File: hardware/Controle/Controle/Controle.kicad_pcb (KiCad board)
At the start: 2 copper layers, 70 x 50 mm, 62 parts, among them J101 USART, J102 ST_LINK, J103 FAN, J104 Switches, J301 RJ45, Q101 BCV27, U201 MCP2561-E-SN, U401 AP1117-3.3, U402 AP1117-5, U403 AP1117-15, U501 STM32F103C8Tx, Y501 8mhz

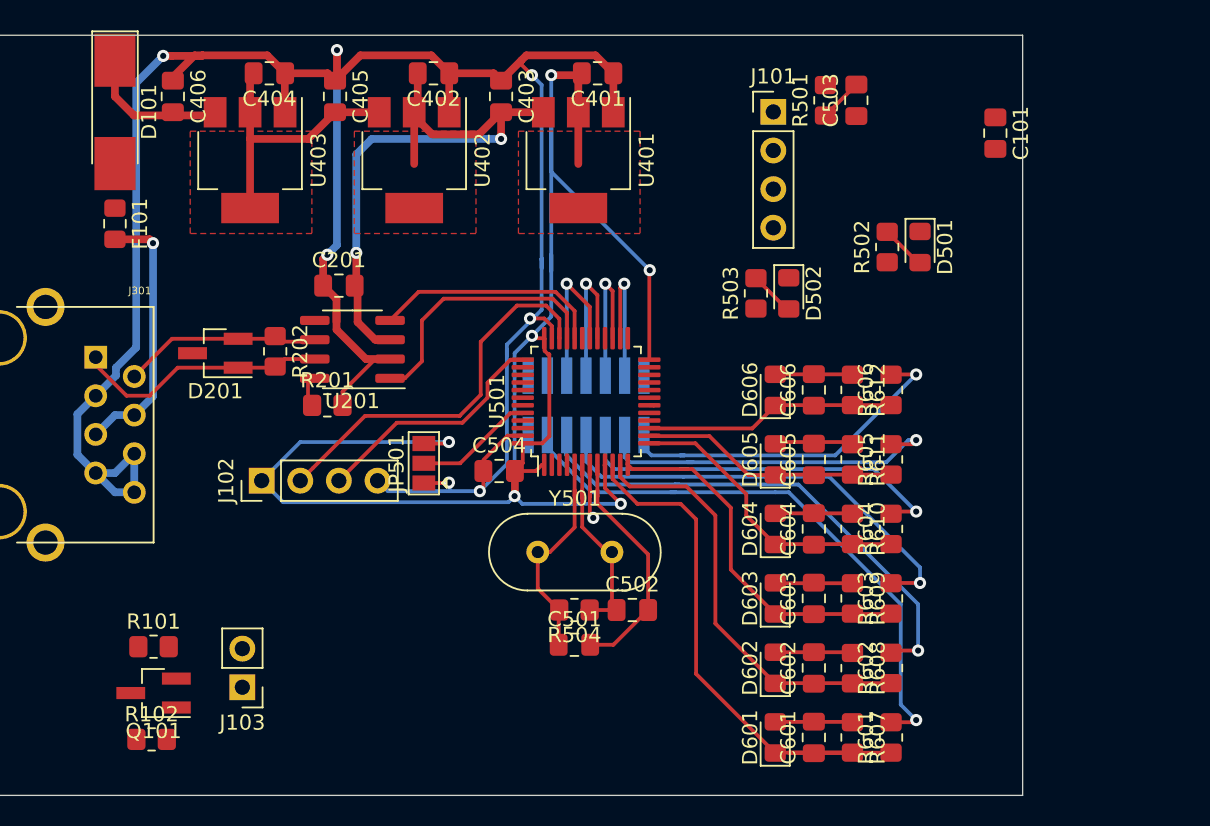
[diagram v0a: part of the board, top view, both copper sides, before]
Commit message: adicionado o TL7726 e modificada a placa
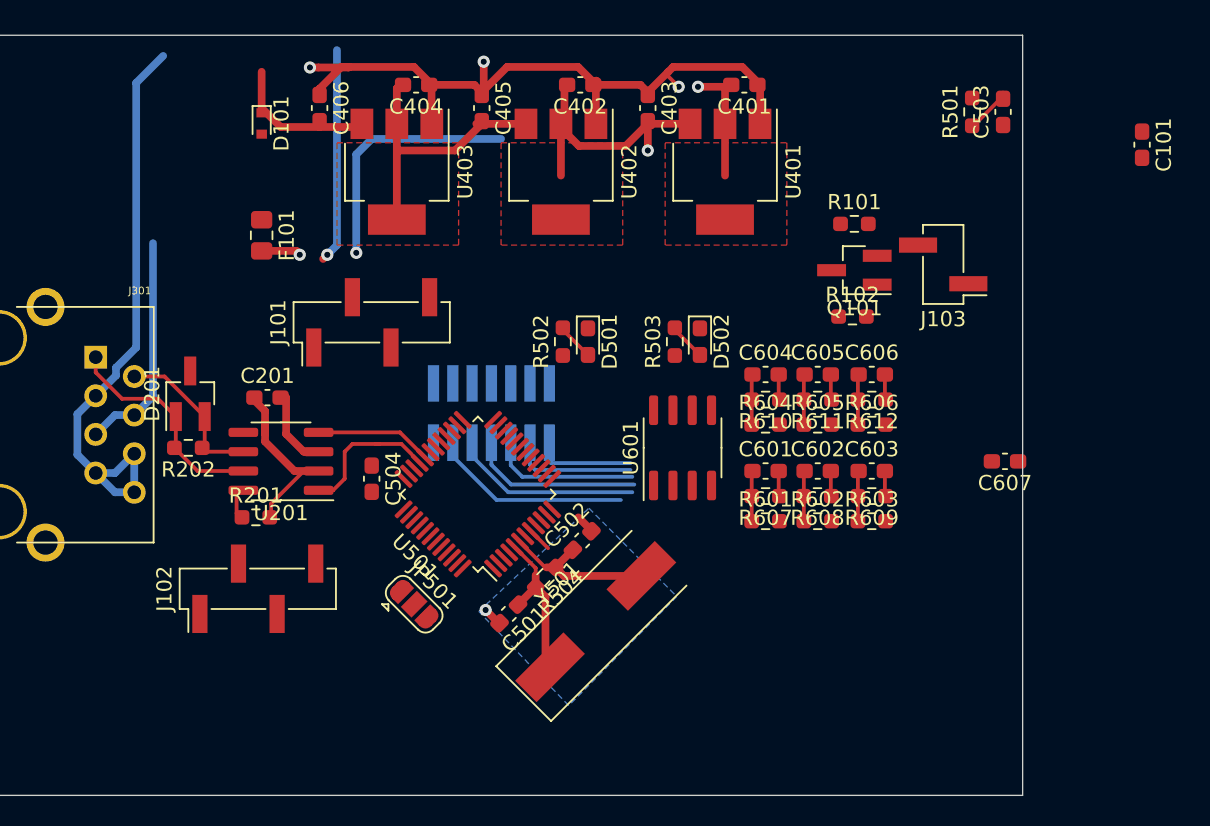
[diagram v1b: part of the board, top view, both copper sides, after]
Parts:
- removed D601, D602, D603, D604, D605, D606: 3v3, Diode_SMD:D_0805_2012Metric_Pad1.15x1.40mm_HandSolder
- added C607: 100n, Capacitor_SMD:C_0603_1608Metric_Pad1.08x0.95mm_HandSolder, F.Cu at (194.6, 73.5)
- added U601: TL7726IDR, Package_SO:SOIC-8_3.9x4.9mm_P1.27mm, F.Cu at (173.4, 72.6)
- C101, C201, C401, C402, C403, C404, C405, C406, C501, C502, C503, C504, C601, C602, C603, C604, C605, C606: footprint Capacitor_SMD:C_0805_2012Metric_Pad1.18x1.45mm_HandSolder -> Capacitor_SMD:C_0603_1608Metric_Pad1.08x0.95mm_HandSolder
- D101: footprint Diode_SMD:D_MELF_Handsoldering -> Diode_SMD:D_SOD-523
- D501, D502: footprint LED_SMD:LED_0805_2012Metric_Pad1.15x1.40mm_HandSolder -> LED_SMD:LED_0603_1608Metric_Pad1.05x0.95mm_HandSolder
- J101, J102: footprint Connector_PinHeader_2.54mm:PinHeader_1x04_P2.54mm_Vertical -> Connector_PinHeader_2.54mm:PinHeader_1x04_P2.54mm_Vertical_SMD_Pin1Left
- J103: footprint Connector_PinHeader_2.54mm:PinHeader_1x02_P2.54mm_Vertical -> Connector_PinHeader_2.54mm:PinHeader_1x02_P2.54mm_Vertical_SMD_Pin1Left
- JP501: footprint Jumper:SolderJumper-3_P1.3mm_Open_Pad1.0x1.5mm -> Jumper:SolderJumper-3_P1.3mm_Open_RoundedPad1.0x1.5mm
- R101, R102, R201, R202, R501, R502, R503, R504, R601, R602, R603, R604, R605, R606, R607, R608, R609, R610, R611, R612: footprint Resistor_SMD:R_0805_2012Metric_Pad1.20x1.40mm_HandSolder -> Resistor_SMD:R_0603_1608Metric_Pad0.98x0.95mm_HandSolder
- Y501: footprint Crystal:Crystal_HC49-U_Vertical -> Crystal:Crystal_SMD_HC49-SD
- moved R102 53.8 mm to (184.5, 64.0)
- moved J103 53.8 mm to (190.5, 60.6)
- moved Q101 53.8 mm to (184.7, 61.0)
- moved R101 53.8 mm to (184.7, 57.9)
- moved J101 29.8 mm to (152.9, 64.4), turned to 90 degrees
- moved D501 22.7 mm to (167.1, 65.7)
- moved R502 22.2 mm to (165.5, 65.7)
- moved C601 17.8 mm to (178.8, 74.2), turned to 0 degrees
- moved R607 16.9 mm to (178.8, 75.8), turned to 180 degrees
- moved R601 16.4 mm to (178.8, 77.5), turned to 0 degrees
- moved C602 13.0 mm to (182.2, 74.2), turned to 0 degrees
- moved R608 11.6 mm to (182.2, 75.8), turned to 180 degrees
- moved R602 10.8 mm to (182.2, 77.5), turned to 0 degrees
- moved R604 10.7 mm to (178.8, 71.1), turned to 0 degrees
- moved C604 10.6 mm to (178.8, 67.8), turned to 0 degrees
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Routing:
- net +3V3: track 114.7 -> 8.13 mm, vias 6 -> 1
- net GND: track 209.9 -> 127.8 mm, vias 7 -> 5
- net /STM32/ADC1_IN0: track 37.3 -> 3.53 mm
- net /STM32/ADC1_IN1: track 28.9 -> 3.25 mm
- net /STM32/SWCLK: track 25.5 -> 0.00 mm
- net /analog/In0: track 38.4 -> 13.1 mm, vias 1 -> 0
- net /analog/In1: track 33.8 -> 12.4 mm, vias 1 -> 0
- net /STM32/ADC1_IN2: track 24.4 -> 3.40 mm
- net /analog/In2: track 29.5 -> 11.4 mm, vias 1 -> 0
- net /STM32/ADCX_IN3: track 19.5 -> 3.25 mm
- net /STM32/SWDIO: track 16.1 -> 0.00 mm
- net /analog/In3: track 25.6 -> 9.80 mm, vias 1 -> 0
- net /analog/In5: track 23.1 -> 7.83 mm, vias 1 -> 0
- net /analog/In4: track 23.5 -> 8.30 mm, vias 1 -> 0
- net /STM32/ADCX_IN4: track 17.0 -> 3.25 mm
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- added copper zone on B.Cu, net GND

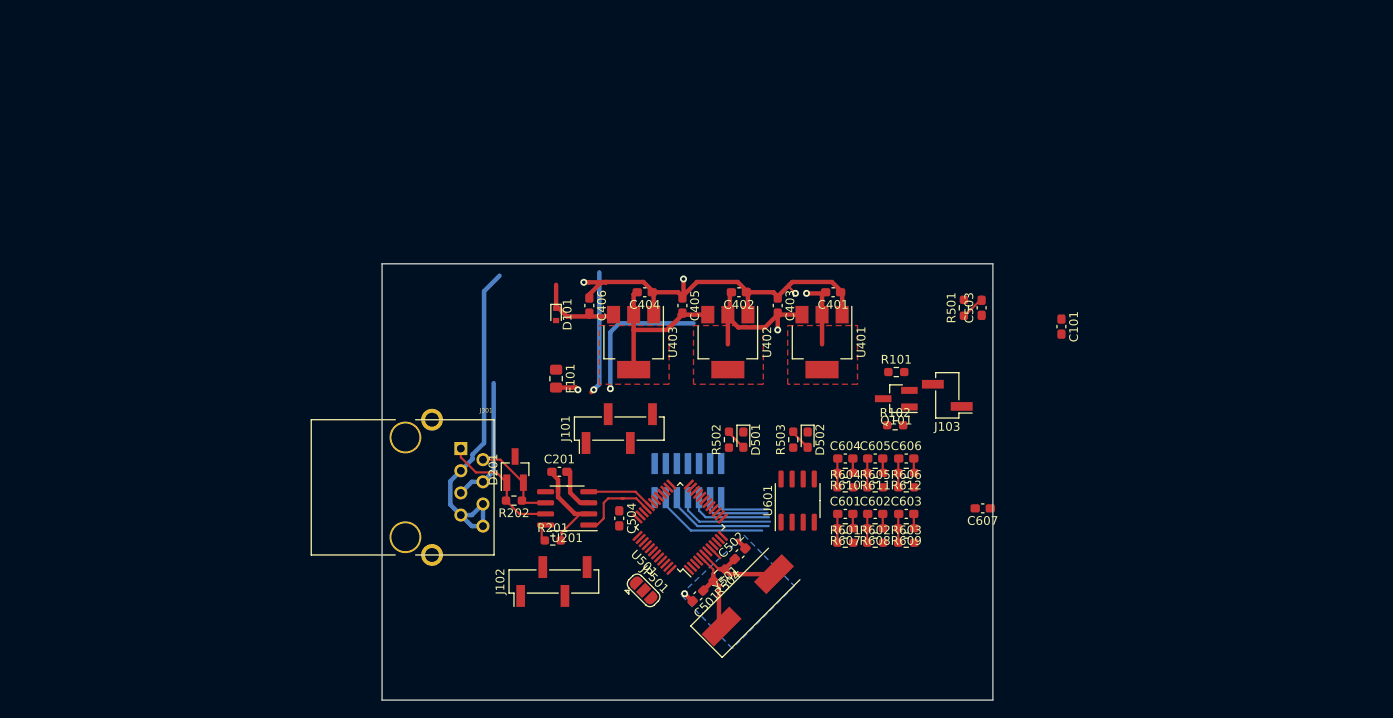
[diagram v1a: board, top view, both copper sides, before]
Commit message: control PCB updated
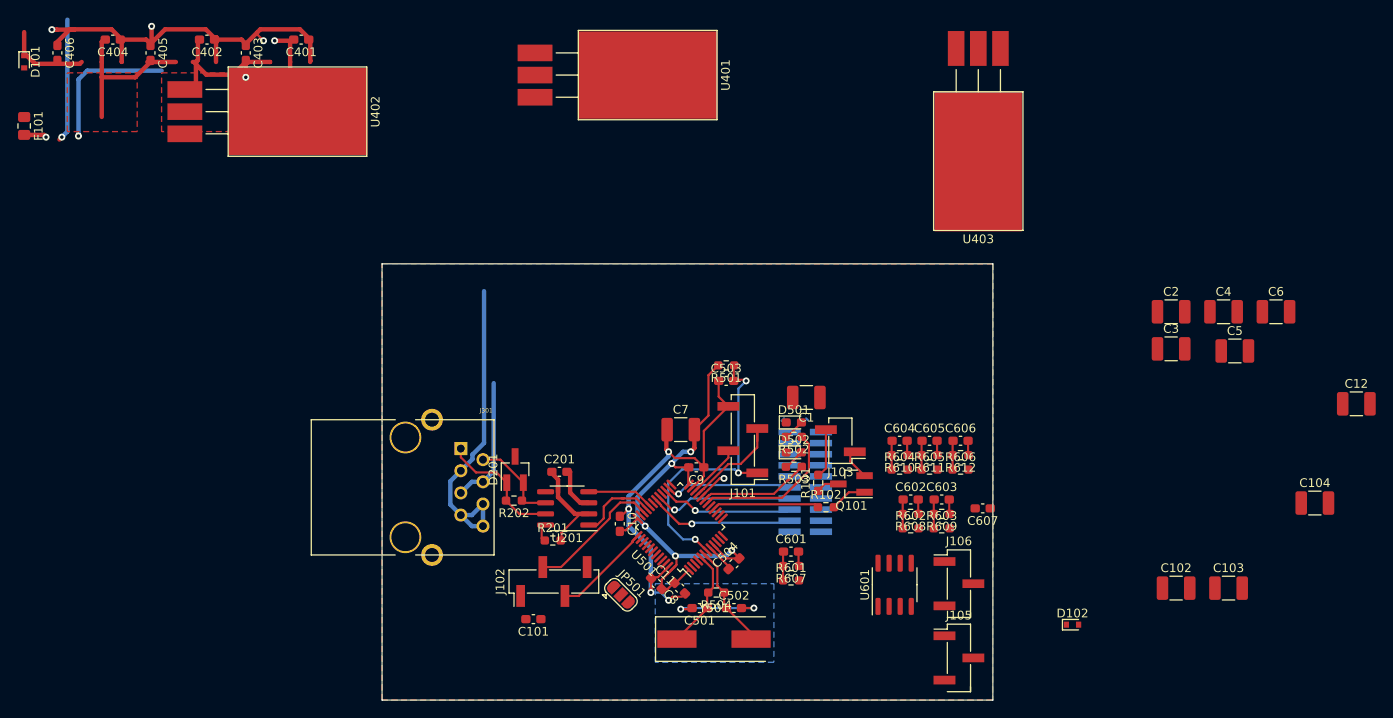
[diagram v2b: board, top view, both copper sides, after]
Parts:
- removed J104: Switches, Connector_PinHeader_1.27mm:PinHeader_2x07_P1.27mm_Vertical_SMD
- added C1: 4.7u, Capacitor_SMD:C_1210_3225Metric_Pad1.33x2.70mm_HandSolder, F.Cu at (174.3, 60.8)
- added C10: 100n, Capacitor_SMD:C_0603_1608Metric_Pad1.08x0.95mm_HandSolder, F.Cu at (153.0, 75.3)
- added C102: 4.7u, Capacitor_SMD:C_1210_3225Metric_Pad1.33x2.70mm_HandSolder, F.Cu at (216.7, 82.7)
- added C103: 4.7u, Capacitor_SMD:C_1210_3225Metric_Pad1.33x2.70mm_HandSolder, F.Cu at (222.7, 82.7)
- added C104: 4.7u, Capacitor_SMD:C_1210_3225Metric_Pad1.33x2.70mm_HandSolder, F.Cu at (232.6, 72.9)
- added C11: 100n, Capacitor_SMD:C_0603_1608Metric_Pad1.08x0.95mm_HandSolder, F.Cu at (157.2, 82.2)
- added C12: 4.7u, Capacitor_SMD:C_1210_3225Metric_Pad1.33x2.70mm_HandSolder, F.Cu at (237.4, 61.6)
- added C2: 4.7u, Capacitor_SMD:C_1210_3225Metric_Pad1.33x2.70mm_HandSolder, F.Cu at (216.2, 51.0)
- added C3: 4.7u, Capacitor_SMD:C_1210_3225Metric_Pad1.33x2.70mm_HandSolder, F.Cu at (216.2, 55.3)
- added C4: 4.7u, Capacitor_SMD:C_1210_3225Metric_Pad1.33x2.70mm_HandSolder, F.Cu at (222.2, 51.0)
- added C5: 4.7u, Capacitor_SMD:C_1210_3225Metric_Pad1.33x2.70mm_HandSolder, F.Cu at (223.5, 55.5)
- added C6: 4.7u, Capacitor_SMD:C_1210_3225Metric_Pad1.33x2.70mm_HandSolder, F.Cu at (228.2, 51.0)
- added C7: 4.7u, Capacitor_SMD:C_1210_3225Metric_Pad1.33x2.70mm_HandSolder, F.Cu at (160.0, 64.5)
- added C8: 100n, Capacitor_SMD:C_0603_1608Metric_Pad1.08x0.95mm_HandSolder, F.Cu at (159.8, 82.7)
- added C9: 100n, Capacitor_SMD:C_0603_1608Metric_Pad1.08x0.95mm_HandSolder, F.Cu at (161.7, 68.8)
- added D102: LL4148, Diode_SMD:D_SOD-523, F.Cu at (204.9, 86.9)
- added J105: Iin_sen, Connector_PinHeader_2.54mm:PinHeader_1x03_P2.54mm_Vertical_SMD_Pin1Left, F.Cu at (191.8, 90.7)
- added J106: Iin_sen, Connector_PinHeader_2.54mm:PinHeader_1x03_P2.54mm_Vertical_SMD_Pin1Left, F.Cu at (191.8, 82.2)
- added J107: Driver-Sense, KicadZeniteSolarLibrary18:PinSocket_2x10_P1.27mm_Vertical_SMD, B.Cu at (174.2, 70.5)
- U401, U402, U403: footprint Package_TO_SOT_SMD:SOT-223-3_TabPin2 -> KicadZeniteSolarLibrary18:TO-220-3_Horizontal_TabDown_SMD
- moved C101 69.2 mm to (143.1, 86.2), turned to 180 degrees
- moved C401 67.5 mm to (116.5, 19.8)
- moved C404 67.5 mm to (94.9, 19.8)
- moved C406 67.5 mm to (88.5, 21.3)
- moved D101 67.5 mm to (84.7, 22.4)
- moved F101 67.5 mm to (84.7, 29.7)
- moved U402 67.5 mm to (104.4, 25.5)
- moved C402 67.5 mm to (105.7, 19.8)
- moved C403 67.5 mm to (110.1, 21.3)
- moved C405 67.5 mm to (99.2, 21.3)
- moved U403 53.1 mm to (196.6, 22.1), turned to 180 degrees
- moved U401 45.8 mm to (144.5, 21.3)
- moved C503 30.4 mm to (165.2, 58.9), turned to 0 degrees
- moved R501 28.0 mm to (165.2, 57.1), turned to 180 degrees
- moved R101 15.5 mm to (175.7, 70.6), turned to 90 degrees
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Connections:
- R601 pad 2: /analog/In0 -> /SL1_sen
- R602 pad 2: /analog/In1 -> /SL2_sen
- R603 pad 2: /analog/In2 -> /Vin_sen
- R604 pad 2: /analog/In3 -> /Temp1
- R605 pad 2: /analog/In4 -> /Iin_sen
- R606 pad 2: /analog/In5 -> /Iout_sen
- U501 pad 26: /STM32/TIM1_CH1N -> /PWM_L1
- U501 pad 27: /STM32/TIM1_CH2N -> /PWM_L2
- U501 pad 29: /STM32/TIM1_CH1 -> /PWM_H1
- U501 pad 30: /STM32/TIM1_CH2 -> /PWM_H2
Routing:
- net GND: track 127.8 -> 194.8 mm, vias 5 -> 11
- net +3V3: track 8.13 -> 65.3 mm, vias 1 -> 6
- net /STM32/RESET: track 3.11 -> 35.3 mm, vias 0 -> 3
- net /STM32/LED0: track 0.00 -> 17.8 mm
- net /PWM_H2: track 0.00 -> 16.7 mm, vias 0 -> 1
- net +5V: track 39.9 -> 23.5 mm, vias 2 -> 1
- net /Powersupply/+18V: track 9.58 -> 26.0 mm, vias 0 -> 1
- net /PWM_H1: track 0.00 -> 16.1 mm, vias 0 -> 1
- net /STM32/SWCLK: track 0.00 -> 15.7 mm
- net /PWM_L1: track 0.00 -> 14.7 mm, vias 0 -> 1
- net /PWM_L2: track 0.00 -> 14.7 mm, vias 0 -> 1
- net /STM32/LED1: track 0.00 -> 13.2 mm
- net /analog/In0: track 13.1 -> 0.00 mm
- net /STM32/USART3_TX: track 0.00 -> 12.6 mm
- net /analog/In1: track 12.4 -> 0.00 mm
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- added copper zone on F.Cu, net GND

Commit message: Update Controle PCB
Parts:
- removed C501, C502: 20p, Capacitor_SMD:C_0603_1608Metric_Pad1.08x0.95mm_HandSolder
- removed R504: 10k, Resistor_SMD:R_0603_1608Metric_Pad0.98x0.95mm_HandSolder
- removed Y501: 8mhz, Crystal:Crystal_SMD_HC49-SD
- D101, D102: value LL4148 -> B0530W; footprint Diode_SMD:D_SOD-523 -> Diode_SMD:D_SOD-123F
- J102: footprint Connector_PinHeader_2.54mm:PinHeader_1x04_P2.54mm_Vertical_SMD_Pin1Left -> Connector_PinHeader_2.54mm:PinHeader_1x05_P2.54mm_Vertical_SMD_Pin1Left
- U401: value AP1117-3.3 -> AMS1117-3.3; footprint KicadZeniteSolarLibrary18:TO-220-3_Horizontal_TabDown_SMD -> Package_TO_SOT_SMD:SOT-223-3_TabPin2
- U402: value AP1117-5 -> AMS1117-5; footprint KicadZeniteSolarLibrary18:TO-220-3_Horizontal_TabDown_SMD -> Package_TO_SOT_SMD:SOT-223-3_TabPin2
- U403: value AP1117-15 -> K78L15-1000R3; footprint KicadZeniteSolarLibrary18:TO-220-3_Horizontal_TabDown_SMD -> KicadZeniteSolarLibrary18:TO-220-3_Horizontal_Tabless_SMD
- U501: value STM32F103C8Tx -> STM32G431CBT6
- moved U402 76.5 mm to (173.9, 57.4)
- moved C406 65.0 mm to (150.3, 41.5)
- moved C404 64.7 mm to (155.6, 42.2)
- moved C405 61.4 mm to (158.6, 37.1)
- moved U403 60.3 mm to (143.1, 49.8), turned to 270 degrees
- moved D101 59.7 mm to (134.1, 55.9), turned to 0 degrees
- moved C104 58.9 mm to (174.2, 65.3), turned to 180 degrees
- moved F101 57.0 mm to (133.9, 58.5), turned to 0 degrees
- moved C402 52.3 mm to (154.4, 38.9)
- moved C403 44.7 mm to (152.7, 34.9)
- moved C401 41.6 mm to (155.6, 33.8)
- moved C103 37.1 mm to (186.5, 90.8), turned to 270 degrees
- moved J101 33.5 mm to (145.1, 90.9), turned to 270 degrees
- moved C503 33.4 mm to (152.6, 89.9)
- moved R501 33.4 mm to (152.6, 88.1)
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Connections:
- J102 pad 4: GND -> /STM32/SWO
- U403 pad 1: GND -> /Powersupply/+18V
- U403 pad 2: +15V -> GND
- U403 pad 3: /Powersupply/+18V -> +15V
- U501 pad 10: /STM32/ADC1_IN0 -> /STM32/ADC1_IN2
- U501 pad 11: /STM32/ADC1_IN1 -> /STM32/ADCX_IN3
- U501 pad 12: /STM32/ADC1_IN2 -> /STM32/ADCX_IN4
- U501 pad 13: /STM32/ADCX_IN3 -> /STM32/ADCX_IN5
- U501 pad 14: /STM32/ADCX_IN4 -> Net-(U501-Pad14)
- U501 pad 15: /STM32/ADCX_IN5 -> Net-(U501-Pad15)
- U501 pad 16: /STM32/FAN -> Net-(U501-Pad16)
- U501 pad 18: /STM32/LED0 -> Net-(U501-Pad18)
- U501 pad 19: /STM32/LED1 -> GND
- U501 pad 20: GND -> +3V3
- U501 pad 21: /STM32/USART3_TX -> +3V3
- U501 pad 22: /STM32/USART3_RX -> Net-(U501-Pad22)
- U501 pad 26: /PWM_L1 -> Net-(U501-Pad26)
- U501 pad 27: /PWM_L2 -> /PWM_L1
- U501 pad 28: Net-(U501-Pad28) -> /PWM_L2
- U501 pad 29: /PWM_H1 -> Net-(U501-Pad29)
- U501 pad 3: Net-(U501-Pad3) -> /STM32/LED0
- U501 pad 30: /PWM_H2 -> /PWM_H1
- U501 pad 31: Net-(U501-Pad31) -> /PWM_H2
- U501 pad 32: /STM32/CAN_RX -> /STM32/FAN
- U501 pad 33: /STM32/CAN_TX -> /STM32/CAN_RX
- U501 pad 34: /STM32/SWCLK -> /STM32/CAN_TX
- U501 pad 38: Net-(U501-Pad38) -> /STM32/SWCLK
- U501 pad 4: Net-(U501-Pad4) -> /STM32/LED1
- U501 pad 40: Net-(U501-Pad40) -> /STM32/SWO
- U501 pad 43: Net-(U501-Pad43) -> /STM32/USART3_TX
- U501 pad 44: /STM32/BOOT0 -> /STM32/USART3_RX
- U501 pad 45: Net-(U501-Pad45) -> /STM32/BOOT0
- U501 pad 5: /STM32/XTAL0 -> Net-(U501-Pad5)
- U501 pad 6: /STM32/XTAL1 -> Net-(U501-Pad6)
- U501 pad 8: GND -> /STM32/ADC1_IN0
- U501 pad 9: +3V3 -> /STM32/ADC1_IN1
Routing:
- net /STM32/RESET: track 35.3 -> 0.00 mm, vias 3 -> 0
- net GND: track 194.8 -> 164.1 mm, vias 11 -> 4
- net /Powersupply/+18V: track 26.0 -> 0.00 mm, vias 1 -> 0
- net +15V: track 18.5 -> 0.00 mm
- net /STM32/LED0: track 17.8 -> 0.00 mm
- net /PWM_H2: track 16.7 -> 0.00 mm, vias 1 -> 0
- net /PWM_H1: track 16.1 -> 0.00 mm, vias 1 -> 0
- net /STM32/SWCLK: track 15.7 -> 0.00 mm
- net +3V3: track 65.3 -> 79.9 mm, vias 6 -> 4
- net /PWM_L2: track 14.7 -> 0.33 mm, vias 1 -> 0
- net /PWM_L1: track 14.7 -> 0.39 mm, vias 1 -> 0
- net /STM32/LED1: track 13.2 -> 0.00 mm
- net /STM32/BOOT0: track 0.00 -> 12.6 mm
- net /STM32/USART3_TX: track 12.6 -> 0.00 mm
- net /STM32/XTAL1: track 12.0 -> 0.00 mm
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- removed copper zone on F.Cu, net +15V
- removed copper zone on F.Cu, net +3V3
- removed copper zone on F.Cu, net +5V

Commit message: first version of layout
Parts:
- removed JP501: Jumper_NC_Dual, Jumper:SolderJumper-3_P1.3mm_Open_RoundedPad1.0x1.5mm
- added C202: 4.7n, Capacitor_SMD:C_0603_1608Metric_Pad1.08x0.95mm_HandSolder, F.Cu at (156.8, 66.4)
- added H101: MountingHole, MountingHole:MountingHole_3.2mm_M3, F.Cu at (129.5, 83.9)
- added H102: MountingHole, MountingHole:MountingHole_3.2mm_M3, F.Cu at (129.2, 58.4)
- added H103: MountingHole, MountingHole:MountingHole_3.2mm_M3, F.Cu at (196.0, 70.6)
- added R103: ?, Resistor_SMD:R_0603_1608Metric_Pad0.98x0.95mm_HandSolder, F.Cu at (157.7, 59.9)
- added R203: 300, Resistor_SMD:R_0603_1608Metric_Pad0.98x0.95mm_HandSolder, F.Cu at (154.2, 69.0)
- added R204: 60, Resistor_SMD:R_0603_1608Metric_Pad0.98x0.95mm_HandSolder, F.Cu at (155.9, 69.0)
- added R205: 60, Resistor_SMD:R_0603_1608Metric_Pad0.98x0.95mm_HandSolder, F.Cu at (153.2, 66.4)
- added R504: BOOT0, Resistor_SMD:R_0402_1005Metric, F.Cu at (171.3, 86.1)
- added R505: 10k, Resistor_SMD:R_0603_1608Metric_Pad0.98x0.95mm_HandSolder, F.Cu at (168.6, 86.2)
- F101: value 500ma -> 1A; footprint Fuse:Fuse_0805_2012Metric_Pad1.15x1.40mm_HandSolder -> Fuse:Fuse_1812_4532Metric_Pad1.30x3.40mm_HandSolder
- moved C6 77.5 mm to (151.6, 62.6), turned to 270 degrees
- moved C5 71.9 mm to (151.6, 57.4), turned to 90 degrees
- moved C12 59.4 mm to (181.5, 81.9), turned to 180 degrees
- moved C401 52.3 mm to (204.0, 53.7), turned to 270 degrees
- moved C403 46.4 mm to (195.1, 53.7)
- moved C402 44.5 mm to (197.2, 51.2), turned to 270 degrees
- moved C4 37.2 mm to (185.0, 51.2), turned to 270 degrees
- moved U401 35.3 mm to (199.6, 57.7)
- moved D102 34.7 mm to (163.5, 61.3), turned to 90 degrees
- moved C404 33.6 mm to (188.0, 51.2), turned to 270 degrees
- moved C103 33.3 mm to (170.5, 61.6), turned to 90 degrees
- moved J105 31.3 mm to (176.2, 63.5)
- moved C102 28.4 mm to (167.1, 61.6)
- moved C3 24.8 mm to (191.7, 51.2), turned to 180 degrees
- moved J106 20.6 mm to (183.2, 63.5)
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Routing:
- net GND: track 164.1 -> 286.6 mm, vias 4 -> 9
- net +15V: track 0.00 -> 40.0 mm
- net /STM32/ADCX_IN3: track 3.25 -> 32.4 mm
- net /STM32/ADC1_IN2: track 3.40 -> 27.5 mm
- net /SL1_sen: track 0.00 -> 21.4 mm, vias 0 -> 1
- net +3V3: track 79.9 -> 60.1 mm, vias 4 -> 5
- net /Vin_sen: track 0.00 -> 18.2 mm, vias 0 -> 1
- net /Temp1: track 0.00 -> 18.0 mm, vias 0 -> 1
- net /SL2_sen: track 0.00 -> 17.7 mm, vias 0 -> 1
- net /canbus/CAN_L: track 10.8 -> 26.8 mm
- net /STM32/ADC1_IN1: track 3.25 -> 18.9 mm
- net /canbus/CAN_H: track 15.2 -> 30.5 mm
- net Net-(C102-Pad2): track 0.00 -> 12.9 mm
- net /STM32/ADC1_IN0: track 3.53 -> 16.2 mm
- net /Powersupply/+18V: track 0.00 -> 10.6 mm
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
